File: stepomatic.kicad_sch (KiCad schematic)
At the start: 24 parts, among them J2 Conn_01x05, J3 I2C, J4 USB_B_Micro, Q1 MMBT3904, Q2 MMBT3904, SW1 SW_Push, U2 AMS1117-3.3, U3 ULN2003A, U4 CH340C, U7 ESP-07

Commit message: Re-layout
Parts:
- removed R3: R_Photo, OptoDevice:R_LDR_5.0x4.1mm_P3mm_Vertical, symbol Device:R_Photo
- added CGQ1: TCRT5000L, footprint:OPTO-TH_TCRT5000L, symbol TCRT5000L:TCRT5000L
- added R3: 10k, footprint:C0402, symbol Device:R
- added U1: HDC1080DMBR, footprint:SENSOR-SMD_HDC1080DMBR, symbol HDC1080DMBR:HDC1080DMBR
- C2, C3, C4: JLC (none) -> C15008; LCSC (none) -> C15008; jlc C15008 -> (none)
- D1: renamed from D?; JLC (none) -> DNP
- H1, H2, H3, H4, JP1, JP2: JLC (none) -> DNP
- J2: JLC (none) -> C265084; LCSC (none) -> C265084; jlc C265084 -> (none)
- J3: JLC (none) -> C545725; LCSC (none) -> C545725; jlc C545725 -> (none)
- J4: JLC (none) -> C136001; LCSC (none) -> C136001; jlc C136001 -> (none)
- Q1, Q2: footprint Package_TO_SOT_SMD:SOT-23 -> footprint:SOT-23-3_L2.9-W1.3-P1.90-LS2.4-BR; JLC (none) -> C20526; LCSC (none) -> C20526; jlc C20526 -> (none)
- R1, R2: footprint Resistor_SMD:R_0201_0603Metric -> footprint:C0402; JLC (none) -> C25752; LCSC (none) -> C25752; jlc C22790 -> (none)
- R4: value 10k -> 105; jlc C25744 -> (none)
- SW1: JLC (none) -> C318884; LCSC (none) -> C318884; jlc C318884 -> (none)
- U2: JLC (none) -> C6186; LCSC (none) -> C6186; jlc C6186 -> (none)
- U3: JLC (none) -> C7512; LCSC (none) -> C7512; jlc C7512 -> (none)
- U4: JLC (none) -> C7464026; LCSC (none) -> C7464026; jlc C7464026 -> (none)
- U7: JLC (none) -> C82894; LCSC (none) -> C82894; jlc C82894 -> (none)
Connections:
- net +3V3: now also R4.2, R3.1, U1.5 (VDD)
- net ADC: now also CGQ1.1 (C), R3.2; no longer JP2.2 (B)
- net GND: now also CGQ1.2 (E), U1.2 (GND); no longer R4.2
- net I2C_SCL: now also U1.6 (SCL)
- net I2C_SDA: now also U1.1 (SDA)
- net at R4.1: now also JP2.2 (B); no longer JP2.1 (A)
- net IR: now reaches U7.11 (GPIO2)
- net IR: now also CGQ1.4 (C)
- new net: CGQ1.3 (A), JP2.1 (A)
- no-connect marks 7 -> 17
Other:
- note added: "Power capacitors The maximum input voltage of the ADC0 pin is 0 to 1V Reset edge switch https://rayshobby.net/wordpress/tips-and-tricks-for-using-esp8266/ Add test points"
- note removed: "Power capacitors The maximum input voltage of the ADC0 pin is 0 to 1V Capacitor footprints Reset edge switch Deep sleep reset pin issue Neopixel TCRT5000 Use LED active LOW DIP Switch https://rayshobby.net/wordpress/tips-and-tricks-for-using-esp8266/"
- company: (none) -> Besmer Labs
- title: (none) -> Stepomatic

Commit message: Prepare for jlc submission
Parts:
- added C?: 100nF, footprint:C0402, symbol CL05B104KO5NNNC:CL05B104KO5NNNC
- added C?: 10uF, footprint:C0402, symbol CL05A106MQ5NUNC:CL05A106MQ5NUNC
- J2: footprint Connector_JST:JST_XH_B5B-XH-A_1x05_P2.50mm_Vertical -> footprint:CONN-TH_B5B-XH-A-LF-SN; JLC C265084 -> C157991; JLC_URL (none) -> https://jlcpcb.com/partdetail/Jst-B5B_EH_LF_SN/C157991; jlc_url https://jlcpcb.com/partdetail/Jst-B5B_EH_LF_SN/C265084 -> (none)
- J3: JLC_URL (none) -> https://jlcpcb.com/partdetail/566826-BM04B_NSHSS_TBT_LF_SN/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; jlc_url https://jlcpcb.com/partdetail/566826-BM04B_NSHSS_TBT_LF_SN/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 -> (none)
- J4: JLC C136001 -> C505111; JLCPosOffset (none) -> -0.25,0; LCSC C136001 -> C505111
- SW1: JLC_URL (none) -> https://jlcpcb.com/partdetail/XkbConnectivity-TS_1187A_B_AB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; jlc_url https://jlcpcb.com/partdetail/XkbConnectivity-TS_1187A_B_AB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 -> (none)
- U2: JLC_URL (none) -> https://jlcpcb.com/partdetail/Advanced_MonolithicSystems-AM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; JlcRotOffset (none) -> 180; jlc_url https://jlcpcb.com/partdetail/Advanced_MonolithicSystems-AM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 -> (none)
- U3: JLC_URL (none) -> https://jlcpcb.com/partdetail/TexasInstruments-ULN2003ADR/C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; JlcRotOffset (none) -> -90; jlc_url https://jlcpcb.com/partdetail/TexasInstruments-ULN2003ADR/C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 -> (none)
- U4: JLC_URL (none) -> https://jlcpcb.com/partdetail/wch_jiangsu_Qin_heng-CH340C/C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; JlcRotOffset (none) -> -90; jlc_url https://jlcpcb.com/partdetail/wch_jiangsu_Qin_heng-CH340C/C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 -> (none)
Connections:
- net +3V3: now also C?.2, C?.2
- net GND: now also C?.1, C?.1
- net STEPPER1: now also U3.4 (I4); no longer U3.1 (I1)
- net STEPPER2: now also U3.5 (I5); no longer U3.2 (I2)
- net STEPPER3: now also U3.6 (I6); no longer U3.3 (I3)
- net STEPPER4: now also U3.7 (I7); no longer U3.4 (I4)
- net at U3.10 (O7): now also J2.2 (Pin_2)
- net at U3.11 (O6): now also J2.3 (Pin_3)
- net at U3.12 (O5): now also J2.4 (Pin_4)
- net at U3.13 (O4): now also J2.5 (Pin_5); no longer J2.2 (Pin_2)
- net at U3.14 (O3): no longer J2.3 (Pin_3)
- net at U3.15 (O2): no longer J2.4 (Pin_4)
- net at U3.16 (O1): no longer J2.5 (Pin_5)
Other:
- moved on the sheet: U3

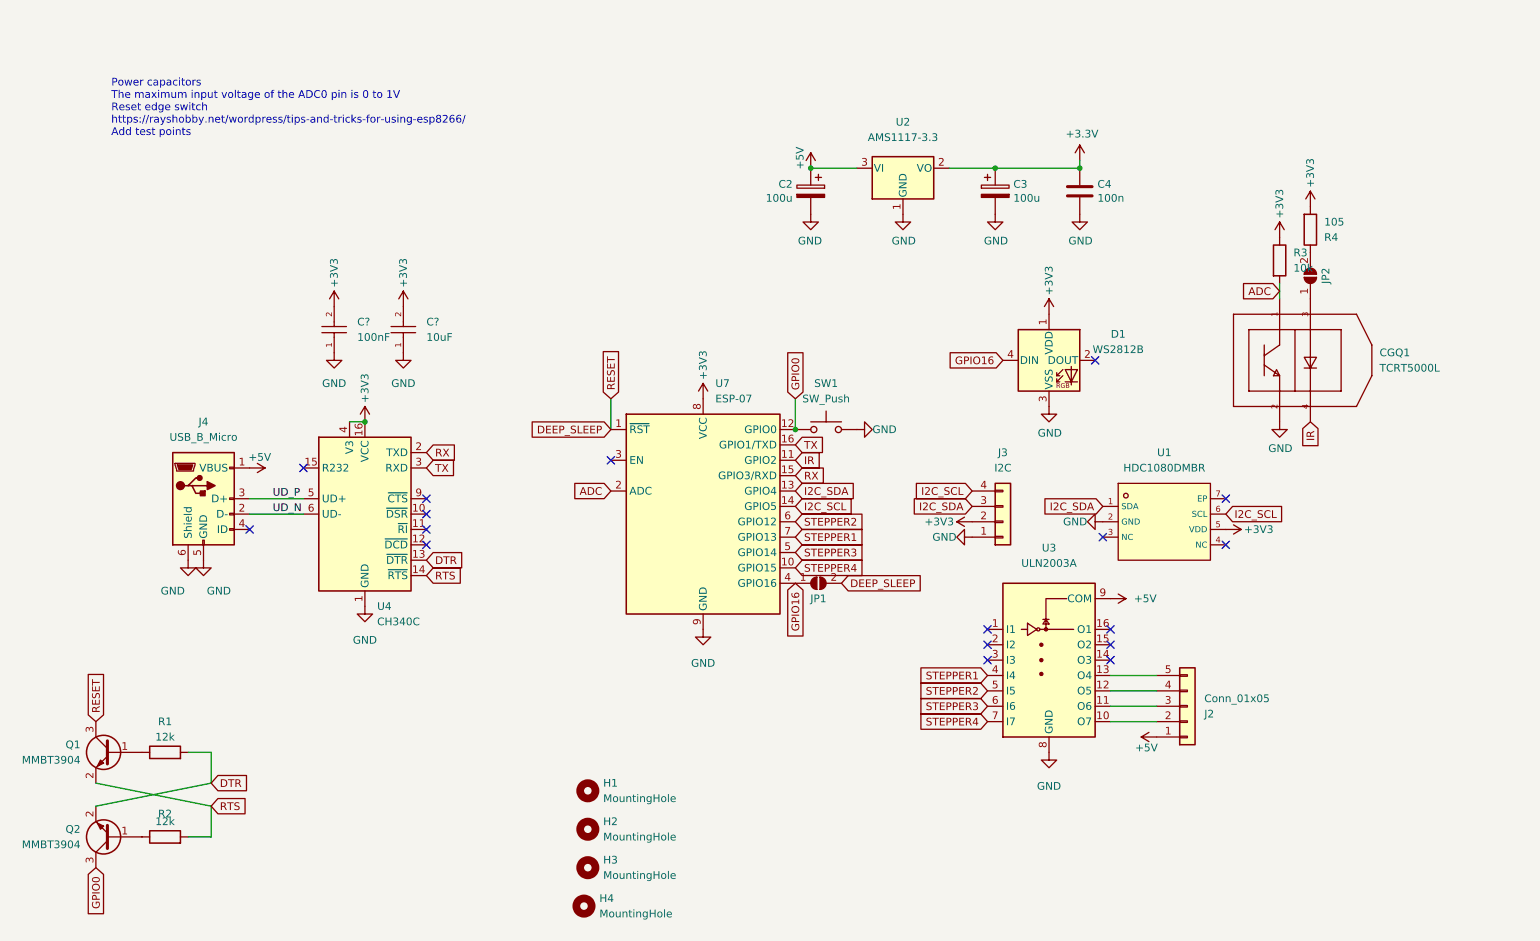
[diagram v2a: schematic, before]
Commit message: Add voltage divider for ADC
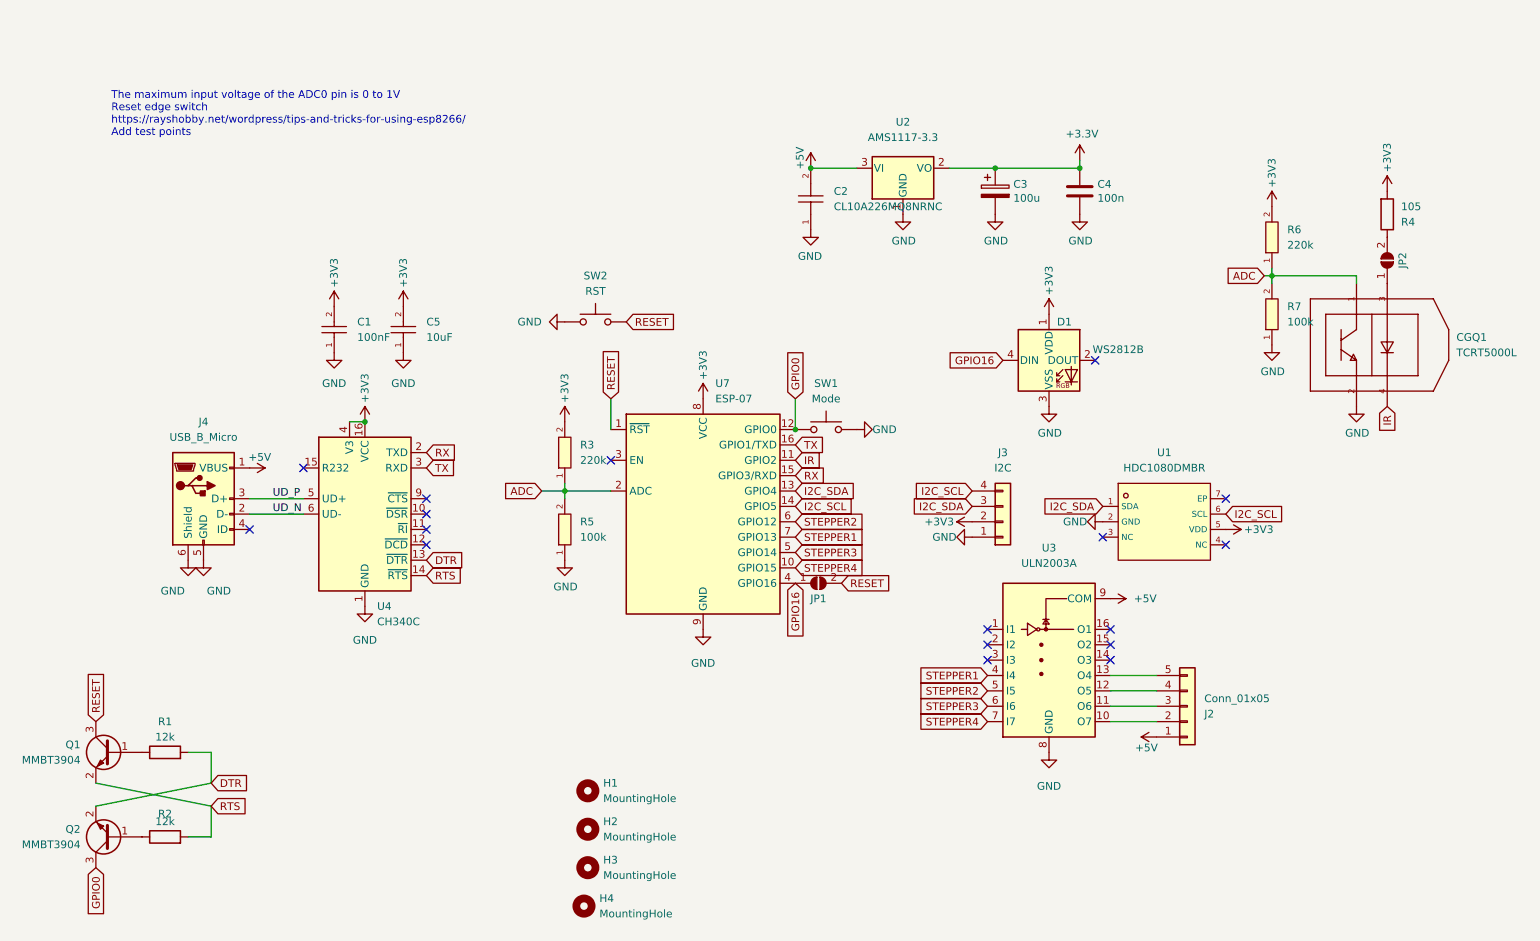
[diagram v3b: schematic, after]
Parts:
- removed C2: 100u, footprint:CASE-B_3528, symbol ESP-12E-breakout-rescue:CP-Device
- removed R3: 10k, footprint:C0402, symbol Device:R
- added C2: CL10A226MQ8NRNC, footprint:C0603, symbol CL10A226MQ8NRNC:CL10A226MQ8NRNC
- added R3, R6: 220k, footprint:R0603, symbol 0603WAF2203T5E:0603WAF2203T5E
- added R5, R7: 100k, footprint:R0603, symbol 0603WAF1003T5E:0603WAF1003T5E
- added SW2: RST, Button_Switch_SMD:SW_SPST_SKQG_WithoutStem, symbol Switch:SW_Push
- SW1: value SW_Push -> Mode
- gave numbers to parts that had none: 2
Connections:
- net +3V3: now also R3.2, R6.2
- net +5V: now also C2.2
- net ADC: now also R3.1, R5.2, R6.1, R7.2
- net GND: now also C2.1, R5.1, R7.1, SW2.1
- net DEEP_SLEEP renamed RESET
- net RESET: now also SW2.2
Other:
- note added: "The maximum input voltage of the ADC0 pin is 0 to 1V Reset edge switch https://rayshobby.net/wordpress/tips-and-tricks-for-using-esp8266/ Add test points"
- note removed: "Power capacitors The maximum input voltage of the ADC0 pin is 0 to 1V Reset edge switch https://rayshobby.net/wordpress/tips-and-tricks-for-using-esp8266/ Add test points"
- moved on the sheet: CGQ1, JP2, R4

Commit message: Add neopixel
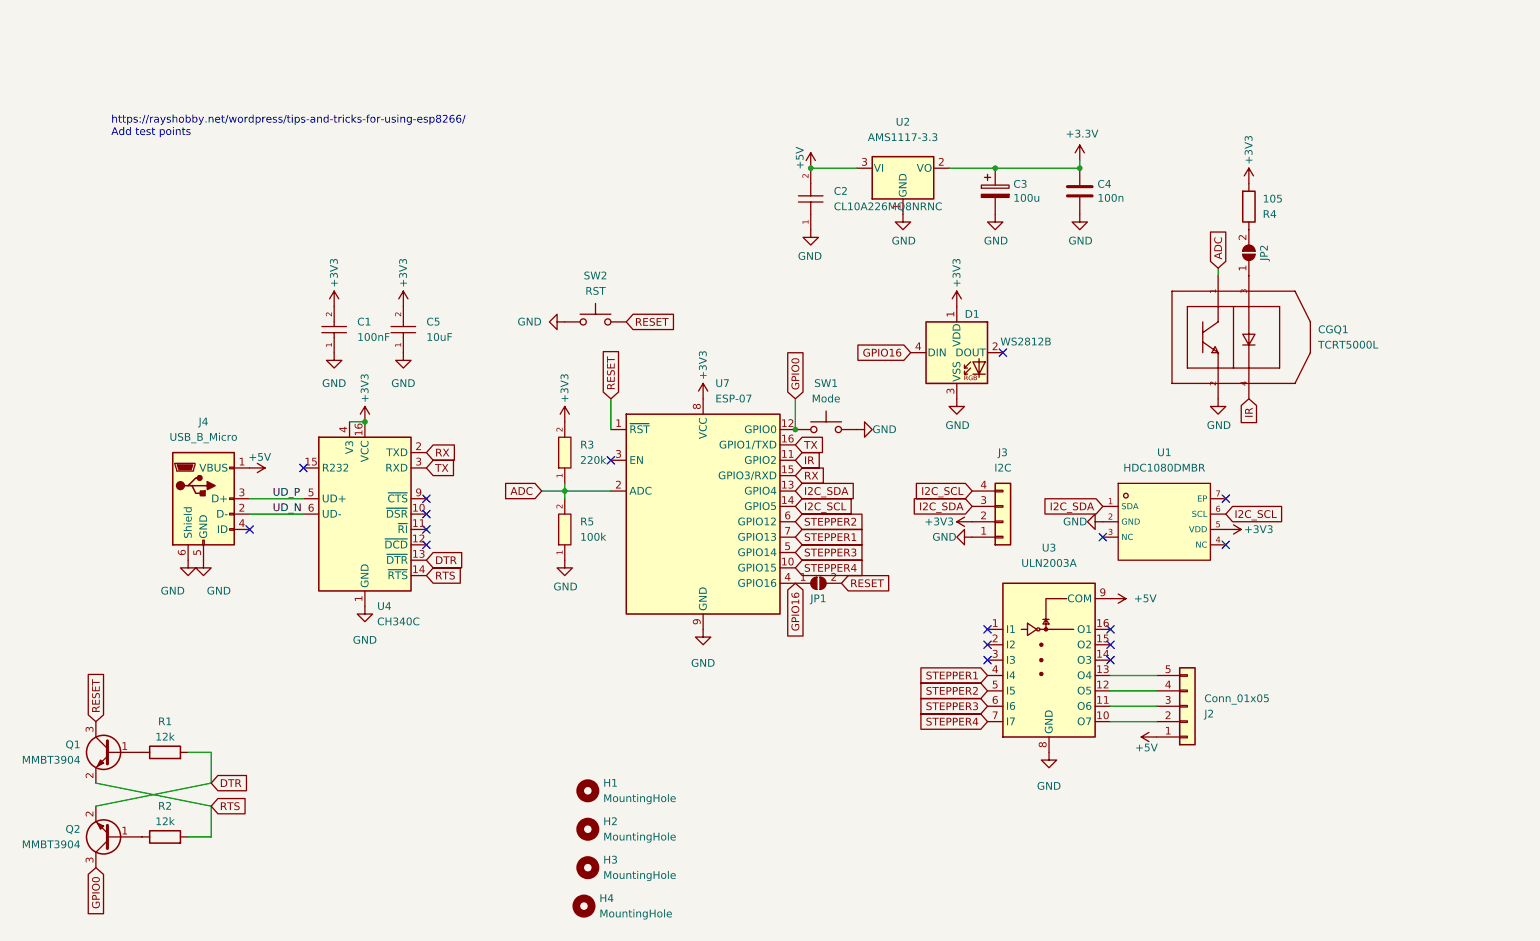
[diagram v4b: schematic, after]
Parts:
- removed R6: 220k, footprint:R0603, symbol 0603WAF2203T5E:0603WAF2203T5E
- removed R7: 100k, footprint:R0603, symbol 0603WAF1003T5E:0603WAF1003T5E
- D1: footprint LED_SMD:LED_WS2812B_PLCC4_5.0x5.0mm_P3.2mm -> footprint:LED-SMD_4P-L5.0-W5.0-BL_XL-5050RGBC; now left out of the parts list
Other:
- note added: "https://rayshobby.net/wordpress/tips-and-tricks-for-using-esp8266/ Add test points"
- note removed: "The maximum input voltage of the ADC0 pin is 0 to 1V Reset edge switch https://rayshobby.net/wordpress/tips-and-tricks-for-using-esp8266/ Add test points"
- moved on the sheet: CGQ1, D1, JP2, R4

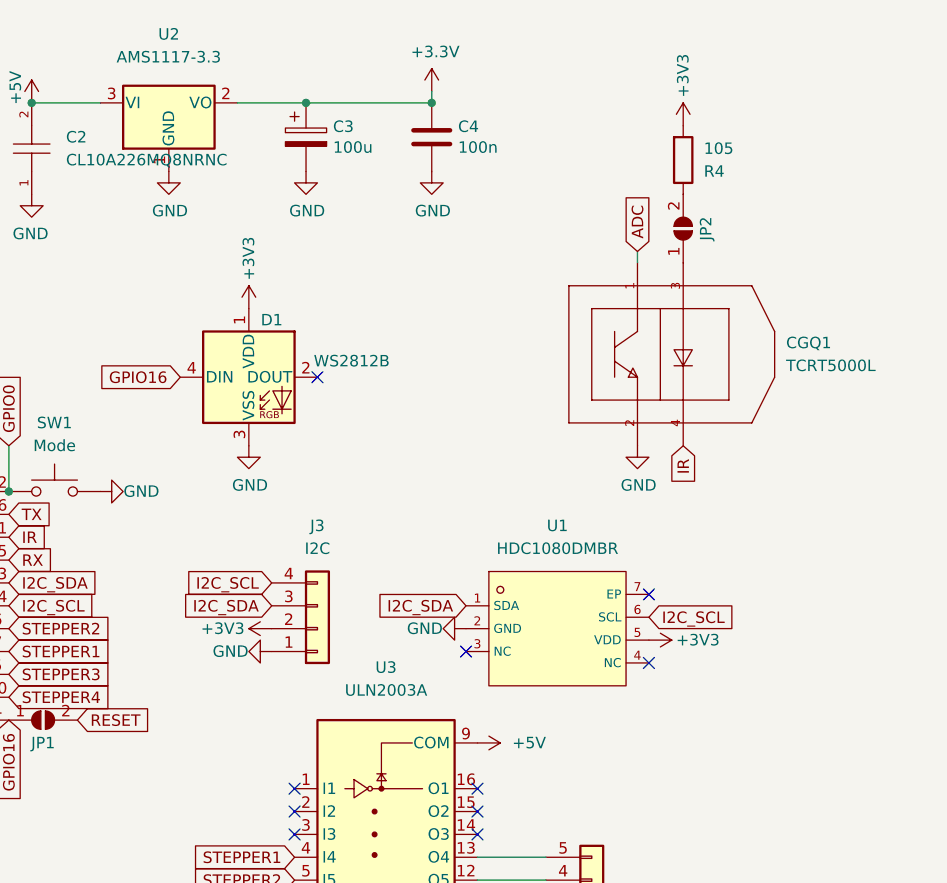
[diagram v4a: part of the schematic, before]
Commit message: Add I2C footprint
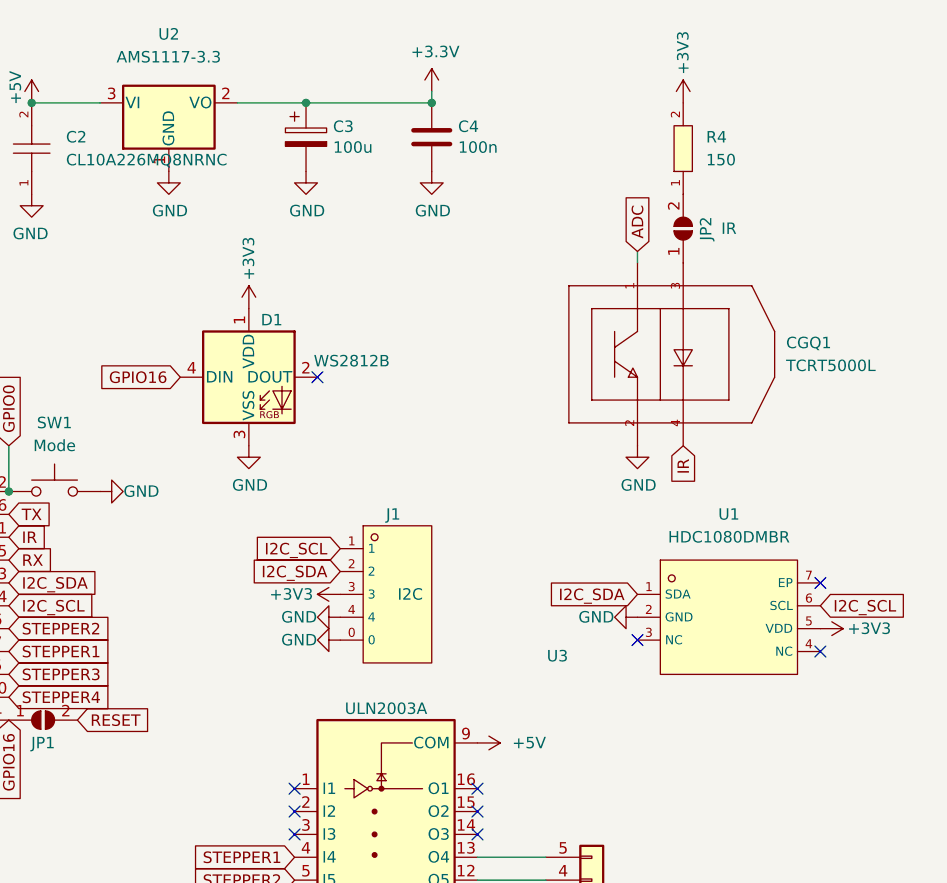
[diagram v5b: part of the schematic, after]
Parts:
- removed J3: I2C, Connector_JST:JST_SH_SM04B-SRSS-TB_1x04-1MP_P1.00mm_Horizontal, symbol Connector_Generic:Conn_01x04
- removed R4: 105, footprint:C0402, symbol Device:R
- added J1: I2C, footprint:CONN-SMD_BM04B-SRSS-TB, symbol BM04B-SRSS-TB(LF)(SN):BM04B-SRSS-TB(LF)(SN)
- added R4: 150, footprint:R0603, symbol 0603WAF1500T5E:0603WAF1500T5E
- C3, C4: JLC C15008 -> (none)
- D1: JLC DNP -> (none); LCSC (none) -> DNP
- H1, H2, H3, H4, JP1: JLC DNP -> (none); LCSC (none) -> DNP; now left out of the parts list
- J2: JLC C157991 -> (none); LCSC C265084 -> C157991
- J4: JLC C505111 -> (none)
- JP2: value brightness -> IR; JLC DNP -> (none); LCSC (none) -> DNP; now left out of the parts list
- Q1, Q2: JLC C20526 -> (none)
- R1, R2: JLC C25752 -> (none)
- SW1, SW2: JLC C318884 -> (none)
- U2: JLC C6186 -> (none)
- U3: JLC C7512 -> (none)
- U4: JLC C7464026 -> (none)
- U7: JLC C82894 -> (none)
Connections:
- net +3V3: now also J1.3, R4.2
- net GND: now also J1.0, J1.4
- net I2C_SCL: now also J1.1
- net I2C_SDA: now also J1.2
- net at JP2.2 (B): now also R4.1
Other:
- moved on the sheet: U1
